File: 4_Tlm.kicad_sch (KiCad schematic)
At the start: 42 parts, among them J502 Conn_Coaxial, SW501 SW_Push, U501 W25Q128JVE, U502 RP2040, U503 Ra-08H, U504 THD-2528-11SD-GF

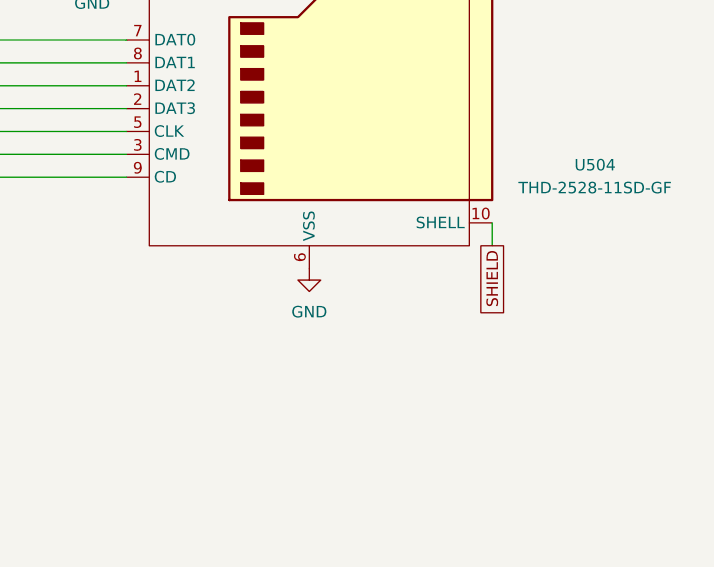
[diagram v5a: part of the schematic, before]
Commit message: Renamed a few nets
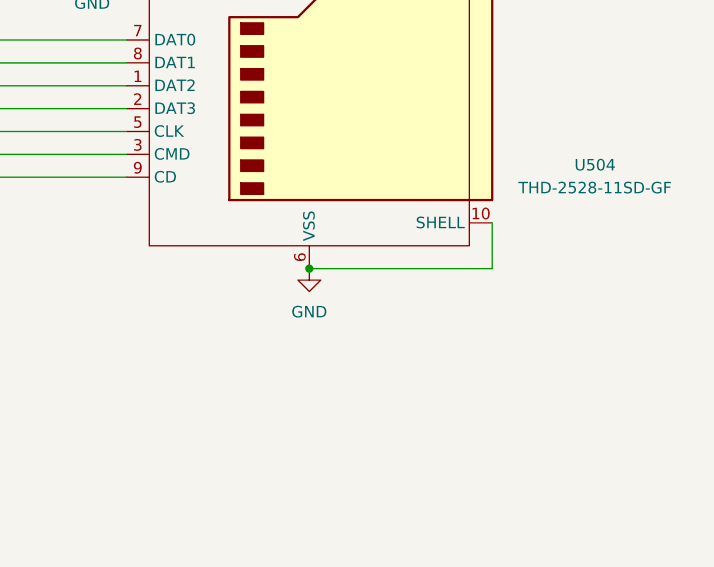
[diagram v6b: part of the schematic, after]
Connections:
- net SHIELD is gone; now on net GND: U504.10 (SHELL), U504.11 (SHELL), U504.12 (SHELL), U504.13 (SHELL)
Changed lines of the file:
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@@
+	)
+	(junction
+		(at 251.46 158.75)
+		(diameter 0)
+		(color 0 0 0 0)
 	)
 	(junction
@@
 	(wire
 		(pts
+			(xy 271.78 153.67) (xy 271.78 158.75)
+		)
+		(stroke
+			(width 0)
+			(type default)
+		)
+	)
+	(wire
+		(pts
 			(xy 173.99 146.05) (xy 231.14 146.05)
 		)
@@
 	(wire
 		(pts
-			(xy 271.78 153.67) (xy 271.78 156.21)
-		)
-		(stroke
-			(width 0)
-			(type default)
-		)
-	)
-	(wire
-		(pts
 			(xy 53.34 128.27) (xy 107.95 128.27)
 		)
@@
 		(pts
 			(xy 130.81 74.93) (xy 130.81 80.01)
+		)
+		(stroke
+			(width 0)
+			(type default)
+		)
+	)
+	(wire
+		(pts
+			(xy 271.78 158.75) (xy 251.46 158.75)
 		)
 		(stroke
@@
 		)
 	)
-	(global_label "SHIELD"
-		(shape passive)
-		(at 271.78 156.21 270)
-		(fields_autoplaced yes)
-		(effects
-			(font
-				(size 1.27 1.27)
-			)
-			(justify right)
-		)
-		(property "Intersheetrefs" "${INTERSHEET_REFS}"
-			(at 271.78 164.6758 90)
-			(hide yes)
-			(show_name no)
-			(do_not_autoplace no)
-			(effects
-				(font
-					(size 1.27 1.27)
-				)
-				(justify right)
-			)
-		)
-	)
